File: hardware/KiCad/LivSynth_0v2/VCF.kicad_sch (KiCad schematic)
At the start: 36 parts, among them J14 Jumper, J8 Jumper, J9 Jumper, Q10 2N3906, Q9 2N3906, U6 TL074, U7 LM13700

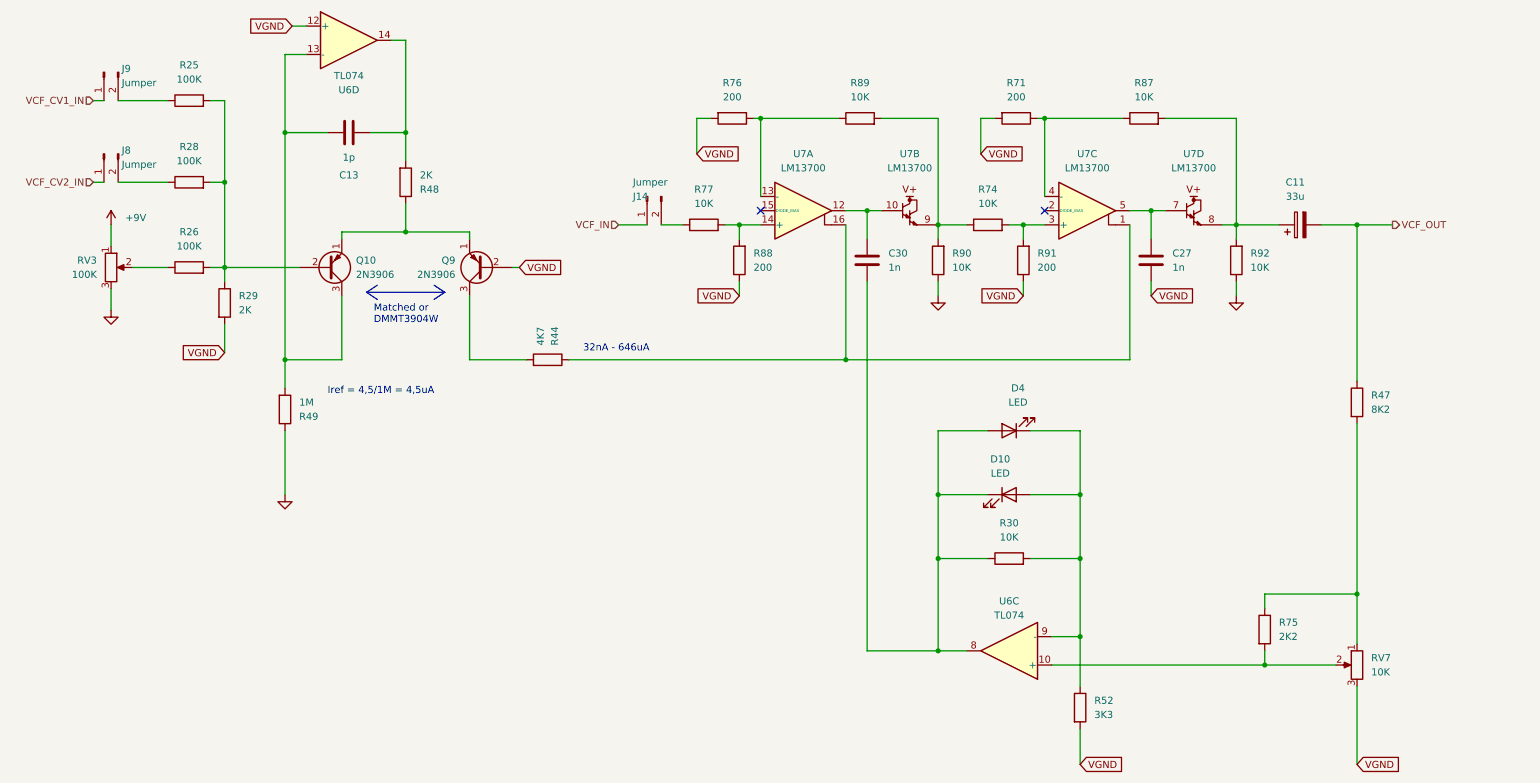
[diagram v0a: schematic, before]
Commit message: Analog redesign:  - Power: Add voltage and current test points  - MCU: use PA11/PA12 for USB DFU interface  - MCU: add NRST reset switch  - Slew: increase portamento cap  - VCO: invert trim pots  - VCF: let resonance kick in earlier  - VCF: invert pots  - VCA: invert trim pot  - EG: full redesign, properly referencing VGND now  - LFO: R61 = 51K  - ModMatrix: add EG attenuverters  - IO: invert pots  - IO: limit output gain for 1W speaker  - IO: connect BTN_SHIFT in gap free order to SR
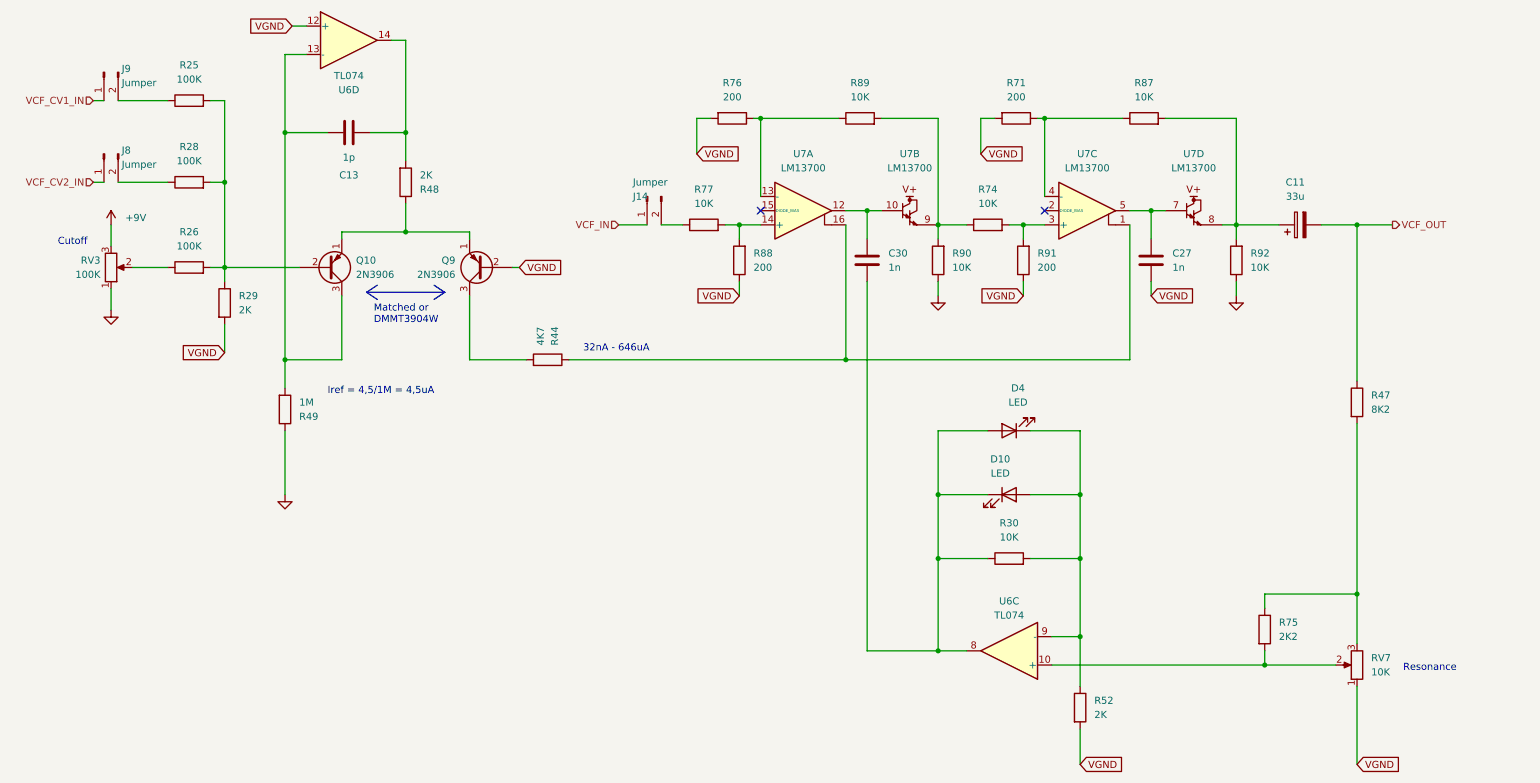
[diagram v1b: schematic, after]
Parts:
- R52: value 3K3 -> 2K
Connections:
- net +9V: now also RV3.3; no longer RV3.1
- net GND: now also RV3.1; no longer RV3.3
- net VGND: now also RV7.1; no longer RV7.3
- net at R47.2, R75.1: now also RV7.3; no longer RV7.1
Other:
- note added: "Cutoff"
- note added: "Resonance"
- moved on the sheet: RV7
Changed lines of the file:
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@@
+    (effects (font (size 1.27 1.27)) (justify left bottom))
+  )
+  (text "Resonance" (at 264.795 143.51 0)
+    (effects (font (size 1.27 1.27)) (justify left bottom))
+  )
+  (text "Cutoff" (at 24.13 67.31 0)
     (effects (font (size 1.27 1.27)) (justify left bottom))
   )
@@
     (effects (font (size 1.27 1.27)) (justify right))
   )
-  (symbol (lib_id "Device:R_Potentiometer") (at 33.655 71.12 0) (unit 1)
-    (in_bom yes) (on_board yes) (fields_autoplaced)
-    (property "Reference" "RV3" (id 0) (at 31.115 69.8499 0)
-      (effects (font (size 1.27 1.27)) (justify right))
-    )
-    (property "Value" "100K" (id 1) (at 31.115 72.3899 0)
+  (symbol (lib_id "Device:R_Potentiometer") (at 33.655 71.12 0) (mirror x) (unit 1)
+    (in_bom yes) (on_board yes) (fields_autoplaced)
+    (property "Reference" "RV3" (id 0) (at 31.75 69.8499 0)
+      (effects (font (size 1.27 1.27)) (justify right))
+    )
+    (property "Value" "100K" (id 1) (at 31.75 72.3899 0)
       (effects (font (size 1.27 1.27)) (justify right))
     )
@@
       (effects (font (size 1.27 1.27)) (justify left))
     )
-    (property "Value" "3K3" (id 1) (at 209.55 151.1299 0)
+    (property "Value" "2K" (id 1) (at 209.55 151.1299 0)
       (effects (font (size 1.27 1.27)) (justify left))
     )
@@
     (pin "2")
   )
-  (symbol (lib_id "Device:R_Potentiometer") (at 256.54 142.24 0) (mirror y) (unit 1)
+  (symbol (lib_id "Device:R_Potentiometer") (at 256.54 142.24 180) (unit 1)
     (in_bom yes) (on_board yes) (fields_autoplaced)
     (property "Reference" "RV7" (id 0) (at 259.08 140.9699 0)

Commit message: Analog Redesign:  - Power: Build ververse polarity protection using P-Mosfet and Zener Diode      - (https://www.youtube.com/watch?v=Ltx4vovY5Z4 - 1:28)  - Power: Build adjustable buck regulator for 8-9V stable voltage source  - PCB: Add location for order number ("JLCJLCJLCJLC")  - General: Add Tooling Holes for PCB assembly  - PCB: check frontend component layout for symmetry  - VCF: fix sound issues  - PCB: Add SloBlo icon  - PCB: Add switch labels to front side  - EG: test new design  - MCU: Add some debug pins
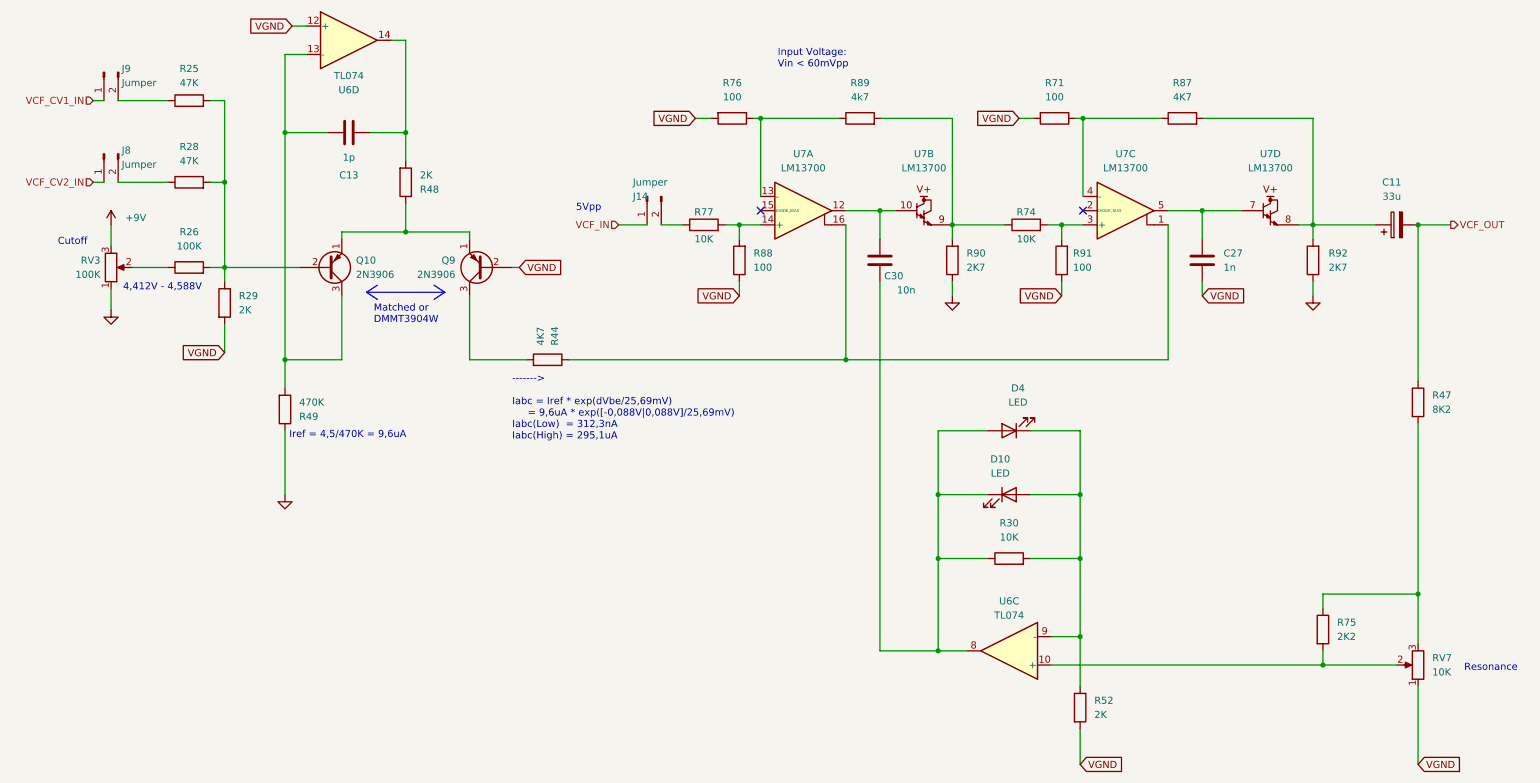
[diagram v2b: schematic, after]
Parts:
- C30: value 1n -> 10n
- R25, R28: value 100K -> 47K
- R49: value 1M -> 470K
- R71, R76, R88, R91: value 200 -> 100
- R87: value 10K -> 4K7
- R89: value 10K -> 4k7
- R90, R92: value 10K -> 2K7
- U6: LCSC (none) -> C2057504
- U7: LCSC (none) -> C4370932
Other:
- note added: "-------> Iabc = Iref * exp(dVbe/25,69mV) = 9,6uA * exp([-0,088V|0,088V]/25,69mV) Iabc(Low) = 312,3nA Iabc(High) = 295,1uA"
- note added: "4,412V - 4,588V"
- note added: "5Vpp"
- note added: "Input Voltage: Vin < 60mVpp"
- note added: "Iref = 4,5/470K = 9,6uA"
- note removed: "32nA - 646uA"
- note removed: "Iref = 4,5/1M = 4,5uA"
- moved on the sheet: C11, C27, C30, R47, R71, R74, R75, R87, R90, R91, R92, RV7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

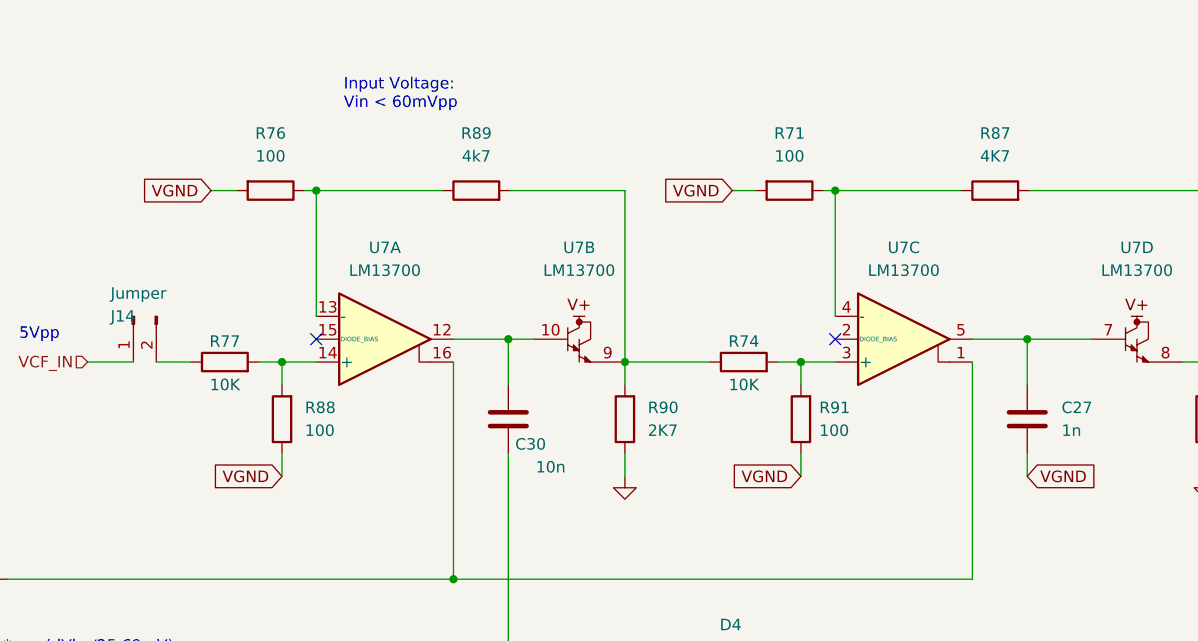
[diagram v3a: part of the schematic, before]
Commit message: LCSC component looked up
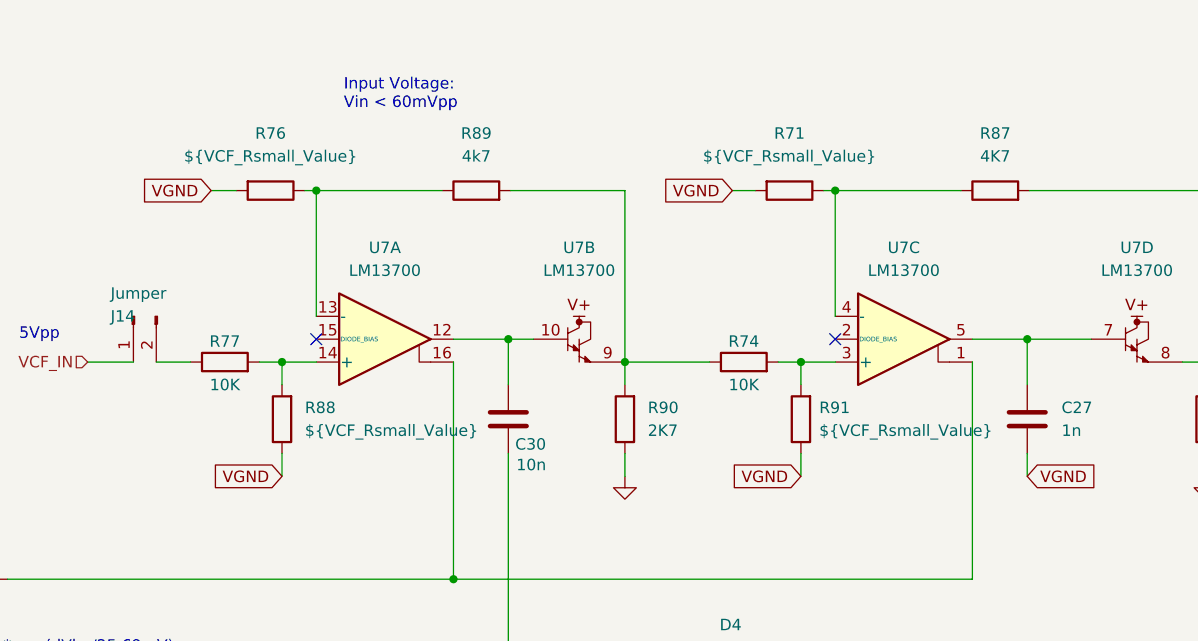
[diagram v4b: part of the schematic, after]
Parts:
- R71, R76, R88, R91: value 100 -> ${VCF_Rsmall_Value}
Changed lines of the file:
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@@
       (effects (font (size 1.27 1.27)) (justify left))
     )
-    (property "Value" "10n" (id 1) (at 174.244 75.184 0)
+    (property "Value" "10n" (id 1) (at 172.085 74.93 0)
       (effects (font (size 1.27 1.27)) (justify left))
     )
@@
     (in_bom yes) (on_board yes) (fields_autoplaced)
     (property "Reference" "R71" (id 0) (at 202.438 38.1 90))
-    (property "Value" "100" (id 1) (at 202.438 40.64 90))
+    (property "Value" "${VCF_Rsmall_Value}" (id 1) (at 202.438 40.64 90))
     (property "Footprint" "Resistor_THT:R_Axial_DIN0207_L6.3mm_D2.5mm_P7.62mm_Horizontal" (id 2) (at 202.438 42.672 90)
       (effects (font (size 1.27 1.27)) hide)
@@
       (effects (font (size 1.27 1.27)) (justify right))
     )
-    (property "Value" "100" (id 1) (at 205.74 71.1199 0)
+    (property "Value" "${VCF_Rsmall_Value}" (id 1) (at 205.74 71.1199 0)
       (effects (font (size 1.27 1.27)) (justify right))
     )
@@
       (effects (font (size 1.27 1.27)) (justify right))
     )
-    (property "Value" "100" (id 1) (at 148.59 71.1199 0)
+    (property "Value" "${VCF_Rsmall_Value}" (id 1) (at 148.59 71.1199 0)
       (effects (font (size 1.27 1.27)) (justify right))
     )
@@
     (in_bom yes) (on_board yes) (fields_autoplaced)
     (property "Reference" "R76" (id 0) (at 144.78 38.1 90))
-    (property "Value" "100" (id 1) (at 144.78 40.64 90))
+    (property "Value" "${VCF_Rsmall_Value}" (id 1) (at 144.78 40.64 90))
     (property "Footprint" "Resistor_THT:R_Axial_DIN0207_L6.3mm_D2.5mm_P7.62mm_Horizontal" (id 2) (at 144.78 42.672 90)
       (effects (font (size 1.27 1.27)) hide)

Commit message: Geographical reannotate
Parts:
- R67: renamed from R71; value ${VCF_Rsmall_Value} -> 100
- R70: renamed from R76; value ${VCF_Rsmall_Value} -> 100
- R75: renamed from R91; value ${VCF_Rsmall_Value} -> 100
- R76: renamed from R88; value ${VCF_Rsmall_Value} -> 100
- renumbered C11 to C10, C27 to C20, C30 to C21, C13 to C8, D4 to D5, J14 to J19, J9 to J8, J8 to J9, Q9 to Q8, Q10 to Q9, R25 to R17, R28 to R18, R26 to R19, R29 to R24, R52 to R31, R48 to R33, R30 to R34, R49 to R43, R44 to R52, R47 to R53, R75 to R55, R74 to R68, R77 to R69, R87 to R74, R89 to R77, R92 to R85, R90 to R86, RV3 to RV5, RV7 to RV9, U6 to U5
